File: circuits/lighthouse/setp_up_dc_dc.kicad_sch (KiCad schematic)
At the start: 8 parts, among them IC1 SX1308

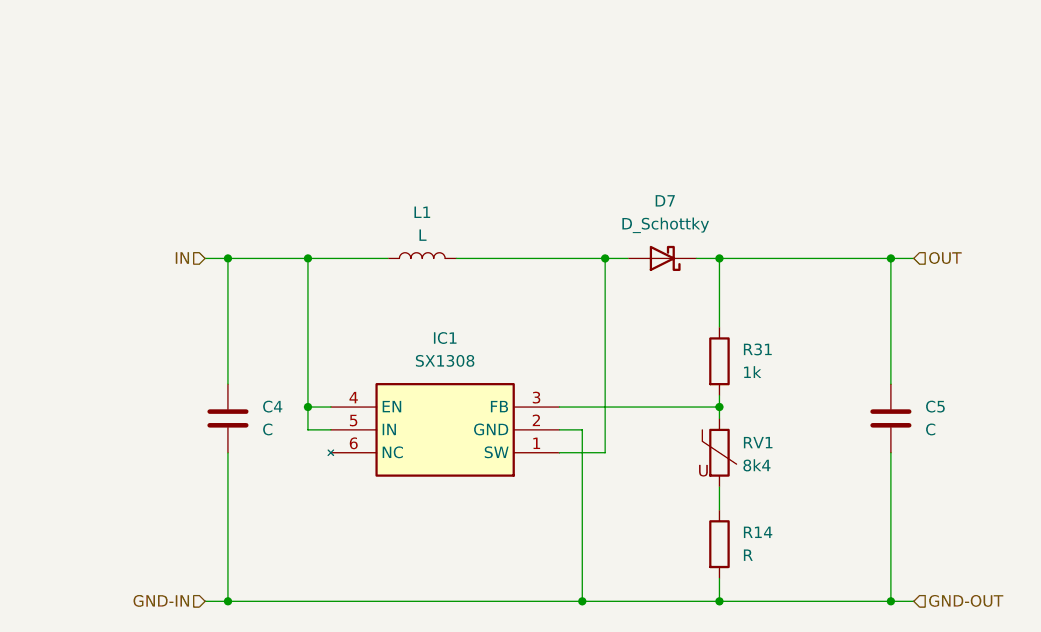
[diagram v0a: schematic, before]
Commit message: The circuit now has all the values in place
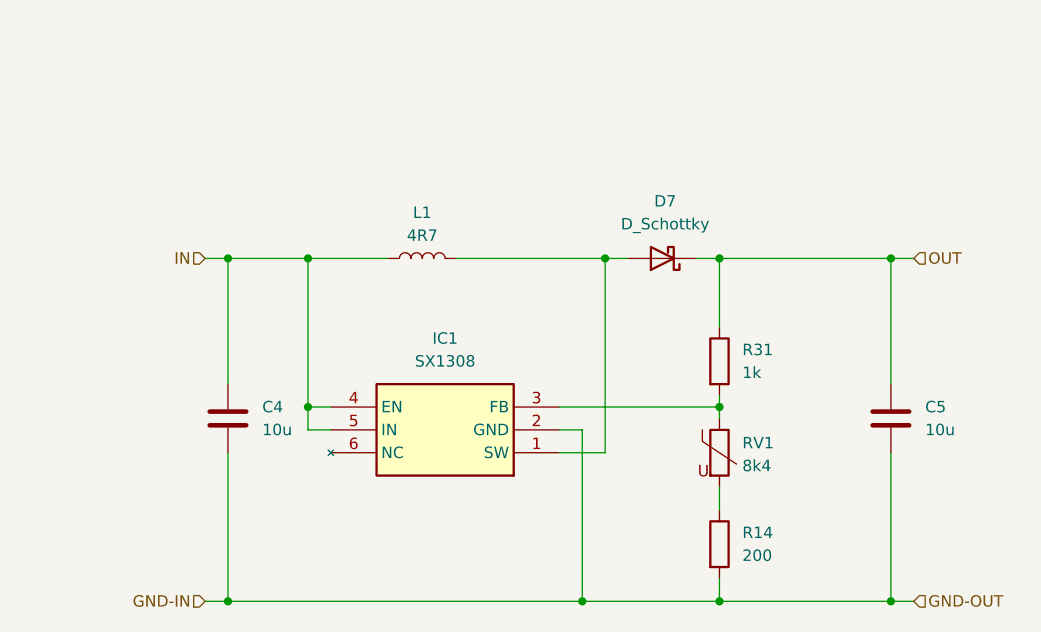
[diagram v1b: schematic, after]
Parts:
- C4, C5: value C -> 10u
- L1: value L -> 4R7
- R14: value R -> 200
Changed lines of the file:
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@@
 			)
 		)
-		(property "Value" "R"
+		(property "Value" "200"
 			(at 135.89 96.5199 0)
 			(effects
@@
 			)
 		)
-		(property "Value" "C"
+		(property "Value" "10u"
 			(at 156.21 82.5499 0)
 			(effects
@@
 			)
 		)
-		(property "Value" "L"
+		(property "Value" "4R7"
 			(at 100.33 60.96 90)
 			(effects
@@
 			)
 		)
-		(property "Value" "C"
+		(property "Value" "10u"
 			(at 82.55 82.5499 0)
 			(effects

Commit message: Cleaned up schematics
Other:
- moved on the sheet: C4, C5, D7, IC1, L1, R14, R31, RV1

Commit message: Safekeeping
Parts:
- removed R31: 1k, Resistor_SMD:R_1206_3216Metric_Pad1.30x1.75mm_HandSolder, symbol Device:R
- removed RV1: 8k4, Varistor:RV_Disc_D7mm_W4.9mm_P5mm, symbol Device:Varistor
- added RV1: W103, 3296W-1-103LF:3296W1503LF, symbol Device:R_Potentiometer_Trim
- R14: value 200 -> 220
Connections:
- net OUT: now also RV1.3
- net at IC1.3 (FB): now also RV1.2
- net at R14.1: now also RV1.1
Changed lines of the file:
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@@
-	)
-	(junction
-		(at 123.19 60.96)
-		(diameter 0)
-		(color 0 0 0 0)
 	)
 	(junction
@@
 	(wire
 		(pts
-			(xy 123.19 69.85) (xy 123.19 72.39)
+			(xy 123.19 64.77) (xy 123.19 72.39)
+		)
+		(stroke
+			(width 0)
+			(type default)
+		)
+	)
+	(wire
+		(pts
+			(xy 105.41 60.96) (xy 119.38 60.96)
 		)
 		(stroke
@@
 	(wire
 		(pts
-			(xy 123.19 60.96) (xy 123.19 62.23)
-		)
-		(stroke
-			(width 0)
-			(type default)
-		)
-	)
-	(wire
-		(pts
 			(xy 123.19 82.55) (xy 142.24 82.55)
 		)
@@
 	(wire
 		(pts
-			(xy 123.19 59.69) (xy 123.19 60.96)
-		)
-		(stroke
-			(width 0)
-			(type default)
-		)
-	)
-	(wire
-		(pts
 			(xy 105.41 63.5) (xy 107.95 63.5)
 		)
@@
 	(wire
 		(pts
-			(xy 123.19 44.45) (xy 123.19 52.07)
+			(xy 123.19 44.45) (xy 123.19 57.15)
 		)
 		(stroke
@@
 		(pts
 			(xy 142.24 66.04) (xy 142.24 82.55)
-		)
-		(stroke
-			(width 0)
-			(type default)
-		)
-	)
-	(wire
-		(pts
-			(xy 105.41 60.96) (xy 123.19 60.96)
 		)
 		(stroke
@@
 			)
 			(justify right)
-		)
-	)
-	(symbol
-		(lib_id "Device:Varistor")
-		(at 123.19 66.04 0)
-		(unit 1)
-		(exclude_from_sim no)
-		(in_bom yes)
-		(on_board yes)
-		(dnp no)
-		(fields_autoplaced yes)
-		(property "Reference" "RV1"
-			(at 125.73 64.9632 0)
-			(effects
-				(font
-					(size 1.27 1.27)
-				)
-				(justify left)
-			)
-		)
-		(property "Value" "8k4"
-			(at 125.73 67.5032 0)
-			(effects
-				(font
-					(size 1.27 1.27)
-				)
-				(justify left)
-			)
-		)
-		(property "Footprint" "Varistor:RV_Disc_D7mm_W4.9mm_P5mm"
-			(at 121.412 66.04 90)
-			(effects
-				(font
-					(size 1.27 1.27)
-				)
-				(hide yes)
-			)
-		)
-		(property "Datasheet" "~"
-			(at 123.19 66.04 0)
-			(effects
-				(font
-					(size 1.27 1.27)
-				)
-				(hide yes)
-			)
-		)
-		(property "Description" "Voltage dependent resistor"
-			(at 123.19 66.04 0)
-			(effects
-				(font
-					(size 1.27 1.27)
-				)
-				(hide yes)
-			)
-		)
-		(property "Sim.Name" "kicad_builtin_varistor"
-			(at 123.19 66.04 0)
-			(effects
-				(font
-					(size 1.27 1.27)
-				)
-				(hide yes)
-			)
-		)
-		(property "Sim.Device" "SUBCKT"
-			(at 123.19 66.04 0)
-			(effects
-				(font
-					(size 1.27 1.27)
-				)
-				(hide yes)
-			)
-		)
-		(property "Sim.Pins" "1=A 2=B"
-			(at 123.19 66.04 0)
-			(effects
-				(font
-					(size 1.27 1.27)
-				)
-				(hide yes)
-			)
-		)
-		(property "Sim.Params" "threshold=1k"
-			(at 123.19 66.04 0)
-			(effects
-				(font
-					(size 1.27 1.27)
-				)
-				(hide yes)
-			)
-		)
-		(property "Sim.Library" "${KICAD9_SYMBOL_DIR}/Simulation_SPICE.sp"
-			(at 123.19 66.04 0)
-			(effects
-				(font
-					(size 1.27 1.27)
-				)
-				(hide yes)
-			)
-		)
-		(pin "2"
-		)
-		(pin "1"
-		)
-		(instances
-			(project ""
-				(path "/7210d03b-7565-45ff-aaca-ad566f37cd67/976e17dd-c379-42b8-98f3-965206833e2e"
-					(reference "RV1")
-					(unit 1)
-				)
-			)
 		)
 	)
@@
 			)
 		)
-		(property "Value" "200"
+		(property "Value" "220"
 			(at 125.73 77.4699 0)
 			(effects
@@
 	)
 	(symbol
-		(lib_id "Device:R")
-		(at 123.19 55.88 0)
+		(lib_id "Device:R_Potentiometer_Trim")
+		(at 123.19 60.96 180)
 		(unit 1)
 		(exclude_from_sim no)
@@
 		(on_board yes)
 		(dnp no)
-		(fields_autoplaced yes)
-		(property "Reference" "R31"
-			(at 125.73 54.6099 0)
-			(effects
-				(font
-					(size 1.27 1.27)
-				)
-				(justify left)
-			)
-		)
-		(property "Value" "1k"
-			(at 125.73 57.1499 0)
-			(effects
-				(font
-					(size 1.27 1.27)
-				)
-				(justify left)
-			)
-		)
-		(property "Footprint" "Resistor_SMD:R_1206_3216Metric_Pad1.30x1.75mm_HandSolder"
-			(at 121.412 55.88 90)
+		(property "Reference" "RV1"
+			(at 125.73 59.69 0)
+			(effects
+				(font
+					(size 1.27 1.27)
+				)
+				(justify right)
+			)
+		)
+		(property "Value" "W103"
+			(at 125.73 62.23 0)
+			(effects
+				(font
+					(size 1.27 1.27)
+				)
+				(justify right)
+			)
+		)
+		(property "Footprint" "3296W-1-103LF:3296W1503LF"
+			(at 123.19 60.96 0)
 			(effects
 				(font
@@
 		)
 		(property "Datasheet" "~"
-			(at 123.19 55.88 0)
-			(effects
-				(font
-					(size 1.27 1.27)
-				)
-				(hide yes)
-			)
-		)
-		(property "Description" "Resistor"
-			(at 123.19 55.88 0)
-			(effects
-				(font
-					(size 1.27 1.27)
-				)
-				(hide yes)
-			)
+			(at 123.19 60.96 0)
+			(effects
+				(font
+					(size 1.27 1.27)
+				)
+				(hide yes)
+			)
+		)
+		(property "Description" "Trim-potentiometer"
+			(at 123.19 60.96 0)
+			(effects
+				(font
+					(size 1.27 1.27)
+				)
+				(hide yes)
+			)
+		)
+		(pin "3"
+		)
+		(pin "2"
 		)
 		(pin "1"
-		)
-		(pin "2"
 		)
 		(instances
 			(project ""
 				(path "/7210d03b-7565-45ff-aaca-ad566f37cd67/976e17dd-c379-42b8-98f3-965206833e2e"
-					(reference "R31")
+					(reference "RV1")
 					(unit 1)
 				)

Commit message: Production ready board
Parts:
- C4: value 10u -> 22u
- D7: value D_Schottky -> SS24A; footprint Diode_SMD:D_2114_3652Metric_Pad1.85x3.75mm_HandSolder -> Diode_SMD:D_SMA
- L1: footprint Inductor_THT:L_Radial_L8.0mm_W8.0mm_P5.00mm_Neosid_SD8 -> IDCP2218ER101M01:IDCP2218ER101M01
- R14: value 220 -> 1k
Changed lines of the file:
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@@
 			)
 		)
-		(property "Value" "D_Schottky"
+		(property "Value" "SS24A"
 			(at 117.1575 40.64 0)
 			(effects
@@
 			)
 		)
-		(property "Footprint" "Diode_SMD:D_2114_3652Metric_Pad1.85x3.75mm_HandSolder"
+		(property "Footprint" "Diode_SMD:D_SMA"
 			(at 116.84 44.45 0)
 			(effects
@@
 			)
 		)
-		(property "Value" "220"
+		(property "Value" "1k"
 			(at 125.73 77.4699 0)
 			(effects
@@
 			)
 		)
-		(property "Footprint" "Inductor_THT:L_Radial_L8.0mm_W8.0mm_P5.00mm_Neosid_SD8"
+		(property "Footprint" "IDCP2218ER101M01:IDCP2218ER101M01"
 			(at 90.17 44.45 0)
 			(effects
@@
 			)
 		)
-		(property "Value" "10u"
+		(property "Value" "22u"
 			(at 72.39 63.4999 0)
 			(effects

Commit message: Schematic title block
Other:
- company: (none) -> Brno University of Technology
- title: (none) -> Step-up DC/DC convertor
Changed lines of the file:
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@@
 	(generator_version "9.0")
 	(paper "A5")
+	(title_block
+		(title "Step-up DC/DC convertor")
+		(date "2026-03-25")
+		(rev "1")
+		(company "Brno University of Technology")
+		(comment 1 "Embedded Implementation of an Attendance System for Integration")
+		(comment 2 "into an Enterprise Application")
+		(comment 3 "Author: Jakub Hloušek")
+		(comment 4 "Supervisor: Ing. Michal Bastl, Ph.D")
+	)
 	(junction
 		(at 123.19 44.45)
